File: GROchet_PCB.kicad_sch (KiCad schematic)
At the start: 15 parts, among them J1 Conn_01x04_Pin, J2 Conn_01x04_Pin, J3 Conn_01x04_Pin, J4 Barrel_Jack_MountingPin, U4 TPS40305DRCR

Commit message: shematic design
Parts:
- removed J4: Barrel_Jack_MountingPin, symbol Connector:Barrel_Jack_MountingPin
- removed U4: TPS40305DRCR, DRC10_2P4X1P65, symbol 2026-01-23_17-05-08:TPS40305DRCR
- added C10, C16: 100uF, Capacitor_SMD:C_1206_3216Metric, symbol Device:C
- added C11, C12, C13, C14, C15: 1uF, Capacitor_SMD:C_0603_1608Metric_Pad1.08x0.95mm_HandSolder, symbol Device:C
- added D1, D2, D3, D4, D5: 1N4148W, Diode_SMD:D_SOD-123, symbol Diode:1N4148W
- added J10, J12, J7, J8, J9: Conn_01x04_Pin, Connector_JST:JST_PH_B4B-PH-K_1x04_P2.00mm_Vertical, symbol Connector:Conn_01x04_Pin
- added J11, J5, J6: Conn_01x03_Pin, Connector_JST:JST_EH_B3B-EH-A_1x03_P2.50mm_Vertical, symbol Connector:Conn_01x03_Pin
- added R10, R13, R14, R16, R18, R19, R20, R8: 1k, Resistor_SMD:R_0603_1608Metric_Pad0.98x0.95mm_HandSolder, symbol Device:R_US
- added R11, R12, R15, R17, R7, R9: 10k, Resistor_SMD:R_0603_1608Metric_Pad0.98x0.95mm_HandSolder, symbol Device:R_US
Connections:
- net +5V: now also C10.1, C16.1, J10.1 (Pin_1), J11.1 (Pin_1), J12.1 (Pin_1), J5.2 (Pin_2), J6.1 (Pin_1), J7.1 (Pin_1), J8.1 (Pin_1), J9.1 (Pin_1), R11.1, R12.1, R15.1, R17.1, R7.1, R9.1
- net GND: now also C10.2, C11.1, C12.1, C13.1, C14.1, C15.1, C16.2, J10.2 (Pin_2), J10.4 (Pin_4), J11.3 (Pin_3), J12.2 (Pin_2), J12.4 (Pin_4), J5.1 (Pin_1), J6.3 (Pin_3), J7.2 (Pin_2), J7.4 (Pin_4), J8.2 (Pin_2), J8.4 (Pin_4), J9.2 (Pin_2), J9.4 (Pin_4)
- net X_DIR: now also A1.D27
- net X_EN: now also A1.D29
- net X_STEP: now also A1.D28
- net X_UART: now also A1.D8, R18.2
- net Y_DIR: now also A1.D30
- net Y_EN: now also A1.D32
- net Y_STEP: now also A1.D31
- net Y_UART: now also A1.D10, R19.2
- net Z_DIR: now also A1.D33
- net Z_EN: now also A1.D35
- net Z_STEP: now also A1.D34
- net Z_UART: now also A1.D12, R20.2
- net at A1.D11: now also R20.1
- net LIMIT_INT: now reaches A1.D2 (D2_INT0)
- net UP_BTN: now reaches A1.D22
- net UP_BTN: now also C11.2, D1.1 (K), R7.2, R8.2
- net LEFT_BTN: now reaches A1.D23
- net LEFT_BTN: now also C13.2, D3.1 (K), R11.2, R13.2
- net RIGHT_BTN: now reaches A1.D24
- net RIGHT_BTN: now also C14.2, D4.1 (K), R12.2, R14.2
- net DOWN_BTN: now reaches A1.D25
- net DOWN_BTN: now also C12.2, D2.1 (K), R10.2, R9.2
- net CONF_BTN: now reaches A1.D26
- net CONF_BTN: now also C15.2, D5.1 (K), R15.2, R16.2
- net BTN_INT: now reaches A1.D3 (D3_INT1)
- net BTN_INT: now also D1.2 (A), D2.2 (A), D3.2 (A), D4.2 (A), D5.2 (A), R17.2
- net X_MIN: now reaches A1.D36
- net X_MAX: now reaches A1.D37
- net Y_MIN: now reaches A1.D38
- net Y_MAX: now reaches A1.D39
- net LED_DATA: now reaches A1.D4
- net LED_DATA: now also J11.2 (Pin_2)
- net Z_MIN: now reaches A1.D40
- net Z_MAX: now reaches A1.D41
- net LED_SCREEN_DATA: now reaches A1.D5
- net LED_SCREEN_DATA: now also J6.2 (Pin_2)
- net SERVO_DATA: now reaches A1.D6
- net SERVO_DATA: now also J5.3 (Pin_3)
- net at A1.D7: now also R18.1
- net at A1.D9: now also R19.1
- new net: J12.3 (Pin_3), R8.1
- new net: J7.3 (Pin_3), R10.1
- new net: J9.3 (Pin_3), R14.1
- new net: J8.3 (Pin_3), R13.1
- new net: J10.3 (Pin_3), R16.1
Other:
- added sheet Limit Switches (limit_switches.kicad_sch)
- added sheet Power (power.kicad_sch)
- note added: "BUTTONS"
- note added: "CLAW SERVO"
- note added: "DC-DC"
- note added: "LEDs"
- note added: "LIMIT SWITCHES"
- note added: "MEGA SHIELD"

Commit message: started pcb layout
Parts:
- added C25: 100uF, Capacitor_SMD:C_1206_3216Metric, symbol Device:C
- added JP7: SolderJumper_3_Bridged12, Jumper:SolderJumper-3_P1.3mm_Bridged12_RoundedPad1.0x1.5mm, symbol Jumper:SolderJumper_3_Bridged12
- J1, J2, J3: footprint Connector_JST:JST_XH_B4B-XH-AM_1x04_P2.50mm_Vertical -> Connector_JST:JST_EH_B4B-EH-A_1x04_P2.50mm_Vertical
- J10, J12, J7, J8, J9: footprint Connector_JST:JST_PH_B4B-PH-K_1x04_P2.00mm_Vertical -> Connector_JST:JST_EH_B4B-EH-A_1x04_P2.50mm_Vertical
- U1, U2, U3: footprint (none) -> BIGTREETECH:TMC2208
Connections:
- net +12V: now also JP7.1 (A)
- net +5V: now also JP7.3 (B); no longer J5.2 (Pin_2)
- net GND: now also U1.14 (CLK), U2.14 (CLK), U3.14 (CLK), C25.2
- net X_UART: now also A1.D12, R20.2; no longer A1.D8, R18.2
- net Z_UART: now also A1.D8, R18.2; no longer A1.D12, R20.2
- new net: C25.1, J5.2 (Pin_2), JP7.2 (C)
- no-connect marks 5 -> 2

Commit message: finished routing
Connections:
- net X_MIN: now also A1.D40; no longer A1.D36
- net Z_MIN: now also A1.D36; no longer A1.D40
- net X_MAX: no longer names the net of A1.D37
- net Y_MAX: no longer names the net of A1.D39
- net Z_MAX: no longer names the net of A1.D41
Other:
- sheet Limit Switches ports: added none; removed X_MAX, Y_MAX, Z_MAX
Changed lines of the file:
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@@
 	(wire
 		(pts
-			(xy 271.78 109.22) (xy 265.43 109.22)
-		)
-		(stroke
-			(width 0)
-			(type default)
-		)
-	)
-	(wire
-		(pts
 			(xy 152.4 137.16) (xy 161.29 137.16)
 		)
@@
 		)
 	)
-	(wire
-		(pts
-			(xy 271.78 106.68) (xy 265.43 106.68)
-		)
-		(stroke
-			(width 0)
-			(type default)
-		)
-	)
 	(polyline
 		(pts
@@
 	(wire
 		(pts
-			(xy 271.78 111.76) (xy 265.43 111.76)
-		)
-		(stroke
-			(width 0)
-			(type default)
-		)
-	)
-	(wire
-		(pts
 			(xy 121.92 24.13) (xy 123.19 24.13)
 		)
@@
 	(wire
 		(pts
-			(xy 271.78 104.14) (xy 265.43 104.14)
-		)
-		(stroke
-			(width 0)
-			(type default)
-		)
-	)
-	(wire
-		(pts
-			(xy 43.18 138.43) (xy 52.07 138.43)
-		)
-		(stroke
-			(width 0)
-			(type default)
-		)
-	)
-	(wire
-		(pts
 			(xy 109.22 140.97) (xy 109.22 138.43)
 		)
@@
 	(wire
 		(pts
-			(xy 271.78 114.3) (xy 265.43 114.3)
-		)
-		(stroke
-			(width 0)
-			(type default)
-		)
-	)
-	(wire
-		(pts
 			(xy 149.86 116.84) (xy 149.86 114.3)
 		)
@@
 	(wire
 		(pts
-			(xy 271.78 116.84) (xy 265.43 116.84)
-		)
-		(stroke
-			(width 0)
-			(type default)
-		)
-	)
-	(wire
-		(pts
-			(xy 43.18 133.35) (xy 52.07 133.35)
-		)
-		(stroke
-			(width 0)
-			(type default)
-		)
-	)
-	(wire
-		(pts
 			(xy 101.6 133.35) (xy 102.87 133.35)
 		)
@@
 	(wire
 		(pts
-			(xy 52.07 143.51) (xy 43.18 143.51)
-		)
-		(stroke
-			(width 0)
-			(type default)
-		)
-	)
-	(wire
-		(pts
 			(xy 31.75 63.5) (xy 48.26 63.5)
 		)
@@
 	(wire
 		(pts
-			(xy 43.18 130.81) (xy 52.07 130.81)
+			(xy 43.18 133.35) (xy 52.07 133.35)
 		)
 		(stroke
@@
 	(wire
 		(pts
-			(xy 43.18 135.89) (xy 52.07 135.89)
+			(xy 43.18 138.43) (xy 52.07 138.43)
 		)
 		(stroke
@@
 	(wire
 		(pts
-			(xy 43.18 140.97) (xy 52.07 140.97)
+			(xy 43.18 143.51) (xy 52.07 143.51)
 		)
 		(stroke
@@
 	)
 	(label "Z_MIN"
-		(at 271.78 114.3 180)
+		(at 265.43 104.14 0)
 		(effects
 			(font
 				(size 1.27 1.27)
 			)
-			(justify right bottom)
+			(justify left bottom)
 		)
 	)
@@
 		)
 	)
-	(label "Y_MAX"
-		(at 271.78 111.76 180)
-		(effects
-			(font
-				(size 1.27 1.27)
-			)
-			(justify right bottom)
-		)
-	)
-	(label "Y_MAX"
-		(at 52.07 138.43 180)
-		(effects
-			(font
-				(size 1.27 1.27)
-			)
-			(justify right bottom)
-		)
-	)
 	(label "LEFT_BTN"
 		(at 152.4 157.48 90)
@@
 		)
 	)
-	(label "Z_MAX"
-		(at 52.07 143.51 180)
-		(effects
-			(font
-				(size 1.27 1.27)
-			)
-			(justify right bottom)
-		)
-	)
 	(label "X_DIR"
 		(at 265.43 81.28 0)
@@
 		)
 	)
-	(label "X_MAX"
-		(at 52.07 133.35 180)
-		(effects
-			(font
-				(size 1.27 1.27)
-			)
-			(justify right bottom)
-		)
-	)
 	(label "LED_DATA"
 		(at 265.43 43.18 0)
@@
 	)
 	(label "Y_MIN"
-		(at 52.07 135.89 180)
+		(at 52.07 138.43 180)
 		(effects
 			(font
@@
 		)
 	)
-	(label "X_MAX"
-		(at 271.78 106.68 180)
-		(effects
-			(font
-				(size 1.27 1.27)
-			)
-			(justify right bottom)
-		)
-	)
 	(label "Z_EN"
 		(at 265.43 101.6 0)
@@
 	)
 	(label "X_MIN"
-		(at 271.78 104.14 180)
+		(at 265.43 114.3 0)
 		(effects
 			(font
 				(size 1.27 1.27)
 			)
-			(justify right bottom)
+			(justify left bottom)
 		)
 	)
@@
 	)
 	(label "Z_MIN"
-		(at 52.07 140.97 180)
+		(at 52.07 143.51 180)
 		(effects
 			(font
@@
 	)
 	(label "X_MIN"
-		(at 52.07 130.81 180)
-		(effects
-			(font
-				(size 1.27 1.27)
-			)
-			(justify right bottom)
-		)
-	)
-	(label "Z_MAX"
-		(at 271.78 116.84 180)
+		(at 52.07 133.35 180)
 		(effects
 			(font
@@
 	)
 	(label "Y_MIN"
-		(at 271.78 109.22 180)
+		(at 265.43 109.22 0)
 		(effects
 			(font
 				(size 1.27 1.27)
 			)
-			(justify right bottom)
+			(justify left bottom)
 		)
 	)
@@
 			)
 		)
-		(pin "X_MAX" output
-			(at 43.18 130.81 0)
-			(effects
-				(font
-					(size 1.27 1.27)
-				)
-				(justify right)
-			)
-		)
 		(pin "X_MIN" output
 			(at 43.18 133.35 0)
@@
 			)
 		)
-		(pin "Y_MAX" output
-			(at 43.18 135.89 0)
-			(effects
-				(font
-					(size 1.27 1.27)
-				)
-				(justify right)
-			)
-		)
 		(pin "Y_MIN" output
 			(at 43.18 138.43 0)
 			(effects
 				(font
-					(size 1.27 1.27)
-				)
-				(justify right)
-			)
-		)
-		(pin "Z_MAX" output
-			(at 43.18 140.97 0)
-			(effects
-				(font

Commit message: aaaaaaaaaaaaaaaaaa
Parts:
- added C20, C21: 10uF, Capacitor_SMD:C_0805_2012Metric, symbol Device:C
- added C22, C26: 470uF, Capacitor_THT:CP_Radial_D8.0mm_P3.50mm, symbol Device:C_Polarized
- added U5: 74LVC1G125, Package_TO_SOT_SMD:SOT-23-5, symbol 74xGxx:74LVC1G125
- added U7: 74LVC1G126, Package_TO_SOT_SMD:SOT-23-5, symbol 74xGxx:74LVC1G126
- A1, C11, C12, C13, C14, C15, U1, U2, U3: now left out of the parts list
- C10, C16: LCSC (none) -> C7432784
- C25: value 100uF -> 10uF; footprint Capacitor_SMD:C_1206_3216Metric -> Capacitor_SMD:C_0805_2012Metric; LCSC (none) -> C6119932
- J1, J10, J12, J2, J3, J7, J8, J9: LCSC (none) -> C160258
- R10, R13, R14, R16, R18, R19, R20, R8: LCSC (none) -> C2907113
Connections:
- net +12V: now also C22.1, C26.1
- net GND: now also C20.2, C21.2, C22.2, C26.2
- net at C25.1, J5.2 (Pin_2), JP7.2 (C): now also C20.1, C21.1
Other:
- moved on the sheet: C10, C11, C12, C13, C14, C15, C16, D1, D2, D3, D4, D5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

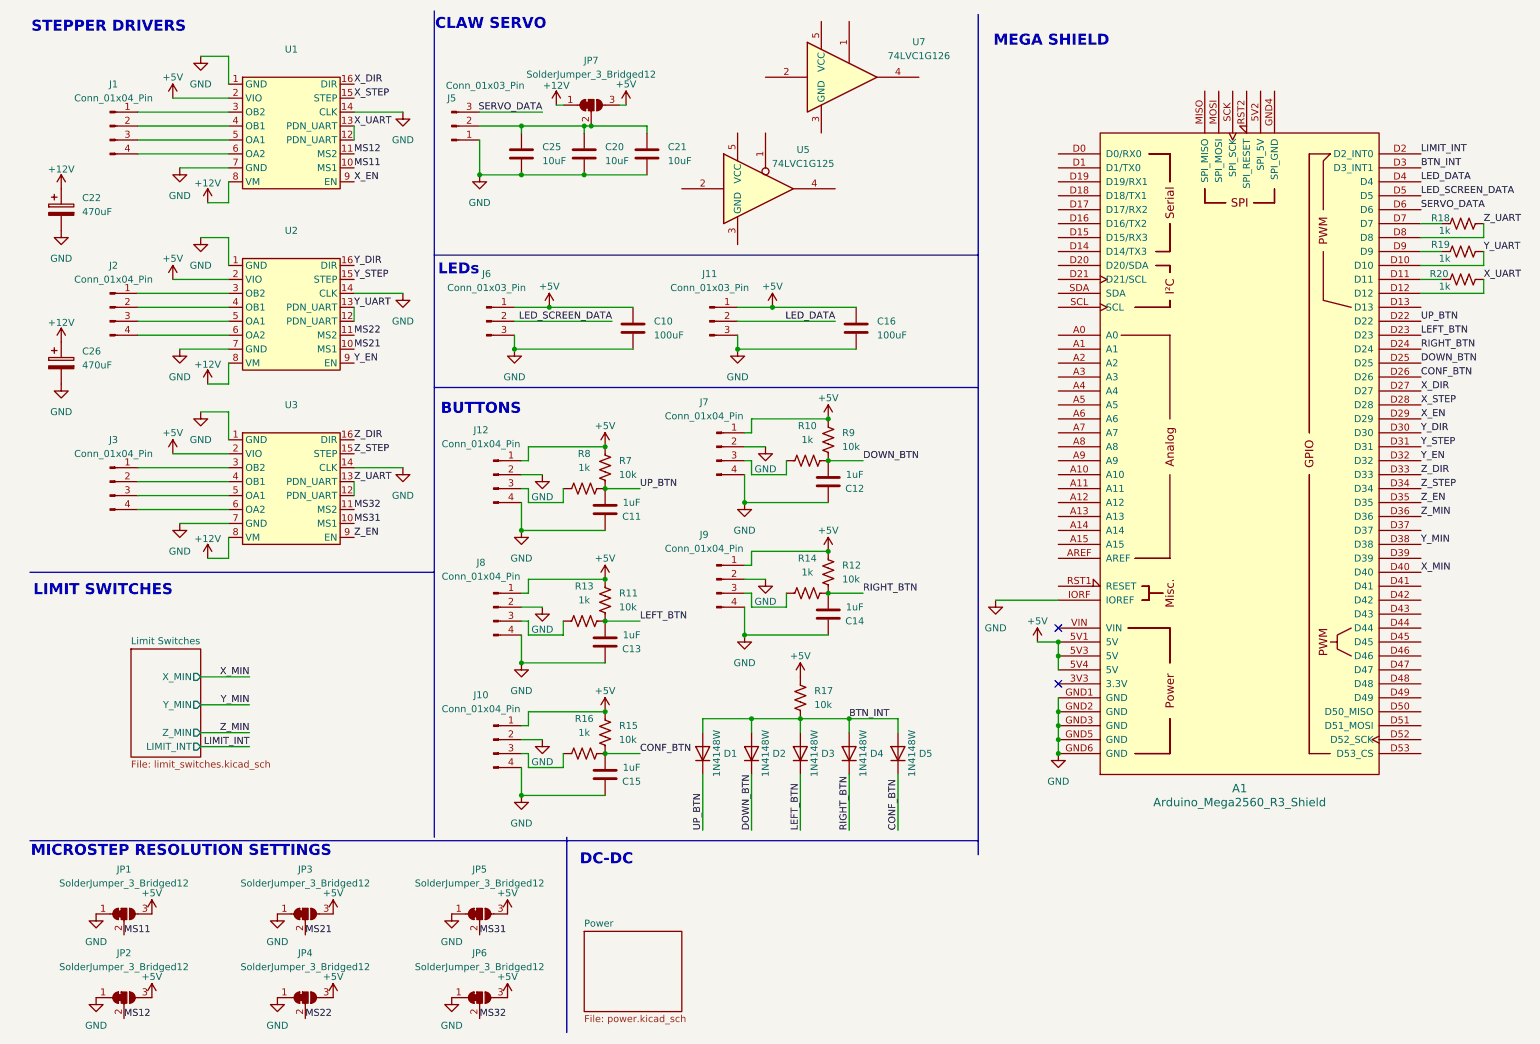
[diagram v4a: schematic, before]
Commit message: DXL Buffer circuit and new prod file
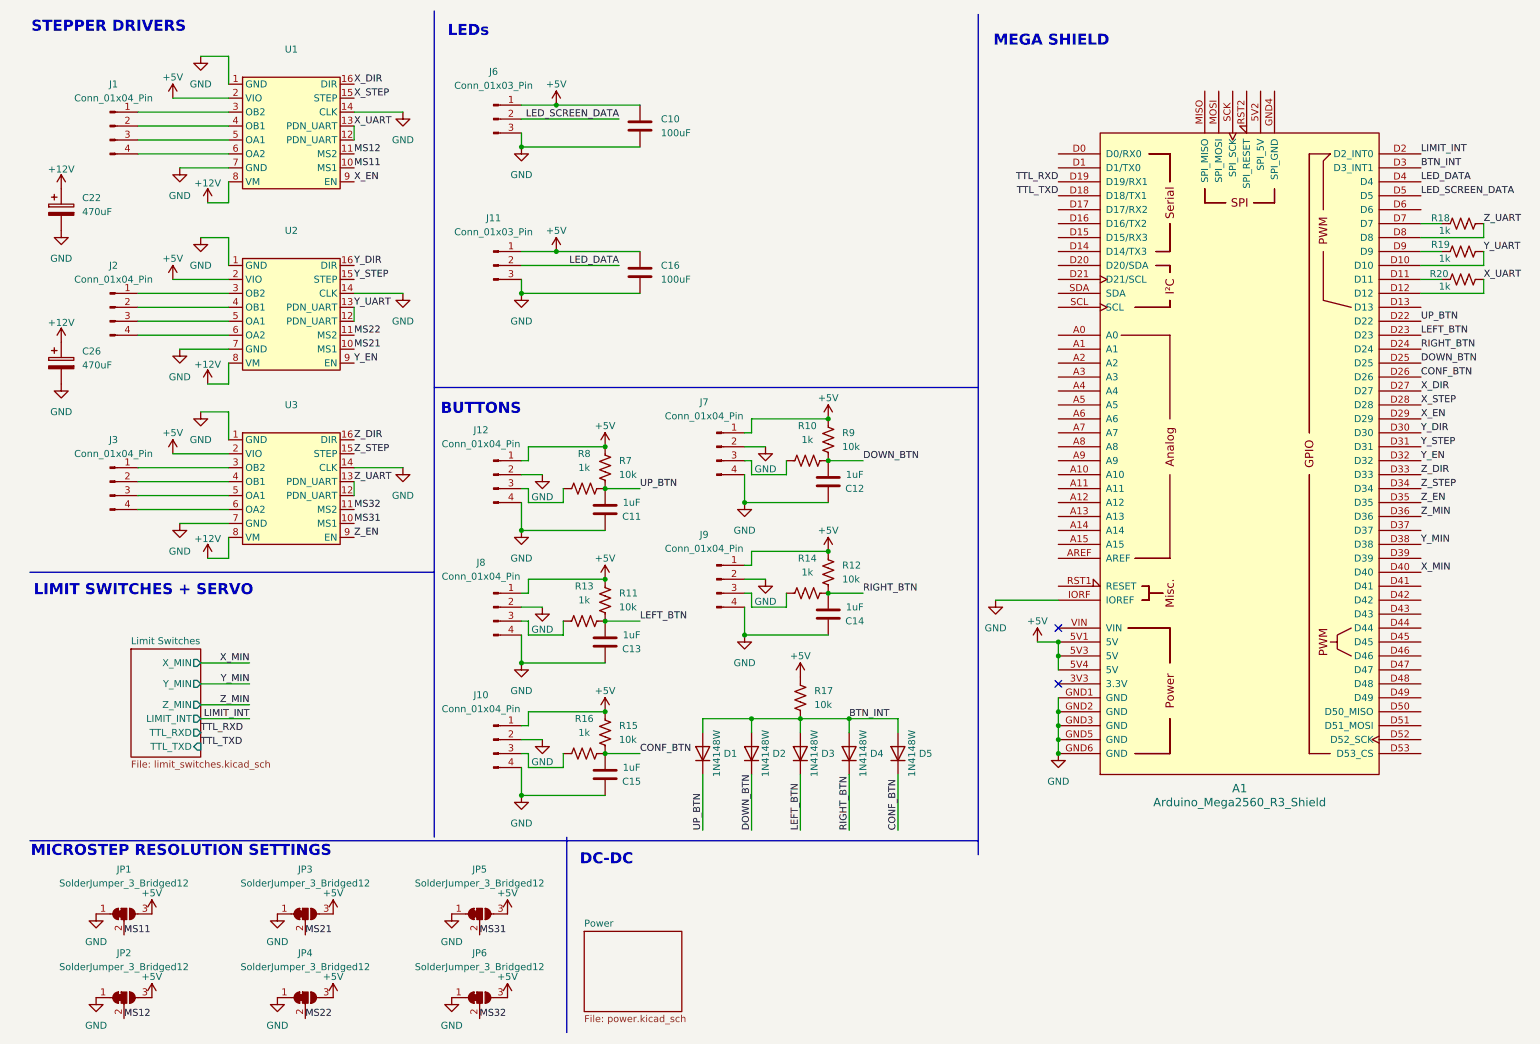
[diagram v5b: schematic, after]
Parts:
- removed C20, C21, C25: 10uF, Capacitor_SMD:C_0805_2012Metric, symbol Device:C
- removed J5: Conn_01x03_Pin, Connector_JST:JST_EH_B3B-EH-A_1x03_P2.50mm_Vertical, symbol Connector:Conn_01x03_Pin
- removed JP7: SolderJumper_3_Bridged12, Jumper:SolderJumper-3_P1.3mm_Bridged12_RoundedPad1.0x1.5mm, symbol Jumper:SolderJumper_3_Bridged12
- removed U5: 74LVC1G125, Package_TO_SOT_SMD:SOT-23-5, symbol 74xGxx:74LVC1G125
- removed U7: 74LVC1G126, Package_TO_SOT_SMD:SOT-23-5, symbol 74xGxx:74LVC1G126
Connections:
- net TTL_TXD: now reaches A1.D18 (D18/TX1)
- net TTL_RXD: now reaches A1.D19 (D19/RX1)
- net SERVO_DATA: no longer names the net of A1.D6
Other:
- sheet Limit Switches ports: added TTL_RXD, TTL_TXD; removed none
- note added: "LIMIT SWITCHES + SERVO"
- note removed: "CLAW SERVO"
- note removed: "LIMIT SWITCHES"
- moved on the sheet: C10, C16, J11, J6

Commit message: added html bom
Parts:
- C11, C12, C13, C14, C15: now in the parts list
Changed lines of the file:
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@@
 		(unit 1)
 		(exclude_from_sim no)
-		(in_bom no)
+		(in_bom yes)
 		(on_board yes)
 		(dnp no)
@@
 		(unit 1)
 		(exclude_from_sim no)
-		(in_bom no)
+		(in_bom yes)
 		(on_board yes)
 		(dnp no)
@@
 		(unit 1)
 		(exclude_from_sim no)
-		(in_bom no)
+		(in_bom yes)
 		(on_board yes)
 		(dnp no)
@@
 		(unit 1)
 		(exclude_from_sim no)
-		(in_bom no)
+		(in_bom yes)
 		(on_board yes)
 		(dnp no)
@@
 		(unit 1)
 		(exclude_from_sim no)
-		(in_bom no)
+		(in_bom yes)
 		(on_board yes)
 		(dnp no)
